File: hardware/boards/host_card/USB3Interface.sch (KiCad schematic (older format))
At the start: 12 parts, among them J2 USB3_Micro_B_Amphenol, J5 Conn_02x04_Odd_Even, U1 ECP5UM5G-381caBGA, U3 CYUSB3014, U6 128MiB

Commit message: Fixed  / updated the ECP5 symbol for the ECP5UM5G-85K
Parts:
- U1: symbol lethalbit:ECP5UM5G-381caBGA -> lethalbit:LFE5UM5G-85F-8BG381I
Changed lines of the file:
@@
 Wire Wire Line
 	5300 6250 5300 6400
-Wire Bus Line
-	3150 3400 3150 4950
-Wire Bus Line
-	9000 2000 9000 3550
 Text Label 11900 2350 2    50   ~ 0
 ALE
@@
 	9000 2000 8650 2000
 $Comp
-L lethalbit:ECP5UM5G-381caBGA U?
+L lethalbit:LFE5UM5G-85F-8BG381I U?
 U 7 1 5FD58016
 P 10450 2200
@@
 NoConn ~ 11350 3550
 NoConn ~ 11350 3650
+Wire Bus Line
+	3150 3400 3150 4950
+Wire Bus Line
+	9000 2000 9000 3550
 $EndSCHEMATC

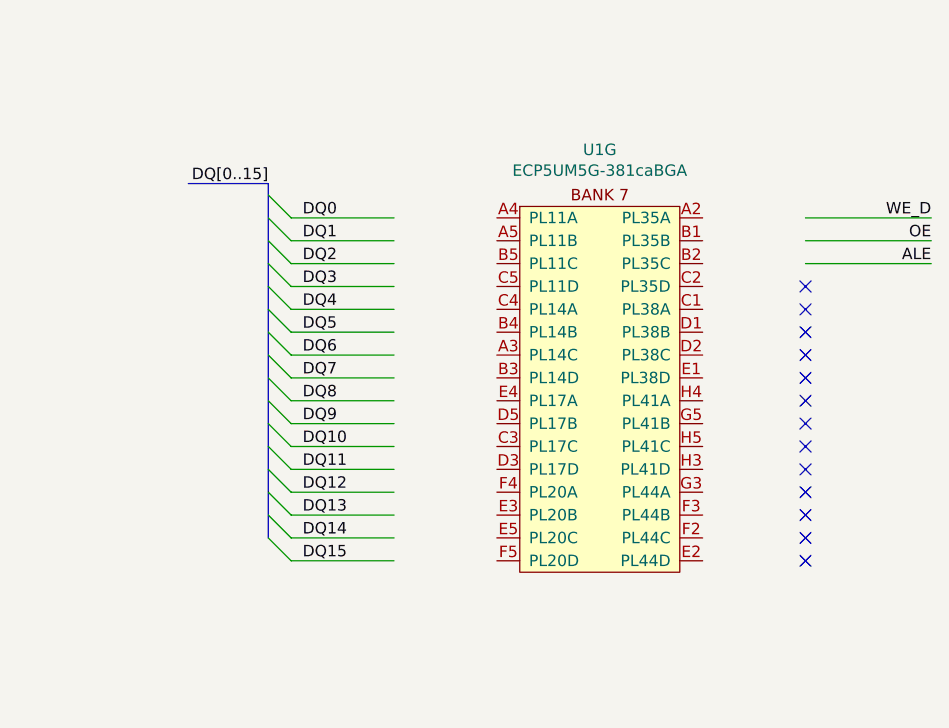
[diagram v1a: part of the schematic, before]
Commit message: Fixed the missing bus connections to the FPGA for the USB3 PHY, and updated the PCB
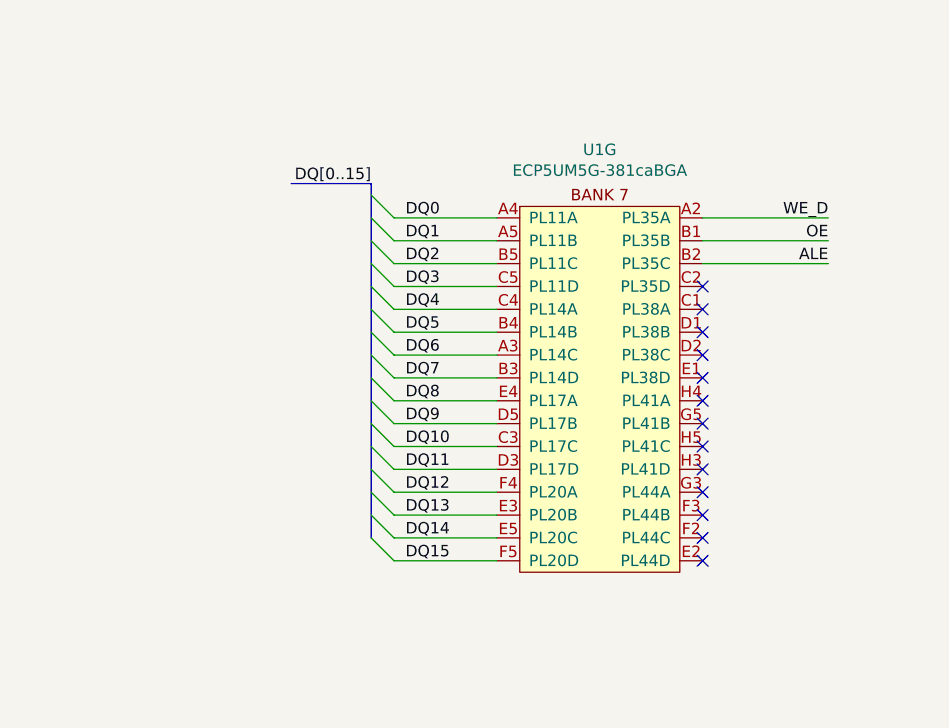
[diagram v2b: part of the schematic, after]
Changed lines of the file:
@@
 Wire Wire Line
 	5300 6250 5300 6400
-Text Label 11900 2350 2    50   ~ 0
+Text Label 11450 2350 2    50   ~ 0
 ALE
 Wire Wire Line
-	11350 2350 11900 2350
-Text Label 11900 2250 2    50   ~ 0
+	10900 2350 11450 2350
+Text Label 11450 2250 2    50   ~ 0
 OE
-Text Label 11900 2150 2    50   ~ 0
+Text Label 11450 2150 2    50   ~ 0
 WE_D
 Wire Wire Line
-	11350 2150 11900 2150
+	10900 2150 11450 2150
 Wire Wire Line
-	11350 2250 11900 2250
-Text Label 9150 2150 0    50   ~ 0
+	10900 2250 11450 2250
+Text Label 9600 2150 0    50   ~ 0
 DQ0
-Text Label 9150 2250 0    50   ~ 0
+Text Label 9600 2250 0    50   ~ 0
 DQ1
-Text Label 9150 2350 0    50   ~ 0
+Text Label 9600 2350 0    50   ~ 0
 DQ2
-Text Label 9150 2450 0    50   ~ 0
+Text Label 9600 2450 0    50   ~ 0
 DQ3
-Text Label 9150 2550 0    50   ~ 0
+Text Label 9600 2550 0    50   ~ 0
 DQ4
-Text Label 9150 2650 0    50   ~ 0
+Text Label 9600 2650 0    50   ~ 0
 DQ5
-Text Label 9150 2750 0    50   ~ 0
+Text Label 9600 2750 0    50   ~ 0
 DQ6
-Text Label 9150 2850 0    50   ~ 0
+Text Label 9600 2850 0    50   ~ 0
 DQ7
-Text Label 9150 2950 0    50   ~ 0
+Text Label 9600 2950 0    50   ~ 0
 DQ8
-Text Label 9150 3050 0    50   ~ 0
+Text Label 9600 3050 0    50   ~ 0
 DQ9
-Text Label 9150 3150 0    50   ~ 0
+Text Label 9600 3150 0    50   ~ 0
 DQ10
-Text Label 9150 3250 0    50   ~ 0
+Text Label 9600 3250 0    50   ~ 0
 DQ11
-Text Label 9150 3350 0    50   ~ 0
+Text Label 9600 3350 0    50   ~ 0
 DQ12
-Text Label 9150 3450 0    50   ~ 0
+Text Label 9600 3450 0    50   ~ 0
 DQ13
-Text Label 9150 3550 0    50   ~ 0
+Text Label 9600 3550 0    50   ~ 0
 DQ14
-Text Label 9150 3650 0    50   ~ 0
+Text Label 9600 3650 0    50   ~ 0
 DQ15
 Wire Wire Line
-	9550 3650 9100 3650
+	10000 3650 9550 3650
 Wire Wire Line
-	9550 3550 9100 3550
+	10000 3550 9550 3550
 Wire Wire Line
-	9550 3450 9100 3450
+	10000 3450 9550 3450
 Wire Wire Line
-	9550 3350 9100 3350
+	10000 3350 9550 3350
 Wire Wire Line
-	9550 3250 9100 3250
+	10000 3250 9550 3250
 Wire Wire Line
-	9550 3150 9100 3150
+	10000 3150 9550 3150
 Wire Wire Line
-	9550 3050 9100 3050
+	10000 3050 9550 3050
 Wire Wire Line
-	9550 2950 9100 2950
+	10000 2950 9550 2950
 Wire Wire Line
-	9550 2850 9100 2850
+	10000 2850 9550 2850
 Wire Wire Line
-	9550 2750 9100 2750
+	10000 2750 9550 2750
 Wire Wire Line
-	9550 2650 9100 2650
+	10000 2650 9550 2650
 Wire Wire Line
-	9550 2550 9100 2550
+	10000 2550 9550 2550
 Wire Wire Line
-	9550 2450 9100 2450
+	10000 2450 9550 2450
 Wire Wire Line
-	9550 2350 9100 2350
+	10000 2350 9550 2350
 Wire Wire Line
-	9550 2250 9100 2250
+	10000 2250 9550 2250
 Wire Wire Line
-	9550 2150 9100 2150
-Text Label 9000 2000 2    50   ~ 0
+	10000 2150 9550 2150
+Text Label 9450 2000 2    50   ~ 0
 DQ[0..15]
 Wire Bus Line
-	9000 2000 8650 2000
+	9450 2000 9100 2000
 $Comp
 L lethalbit:LFE5UM5G-85F-8BG381I U?
@@
 $EndComp
 Entry Wire Line
-	9000 2050 9100 2150
+	9450 2050 9550 2150
 Entry Wire Line
-	9000 2150 9100 2250
+	9450 2150 9550 2250
 Entry Wire Line
-	9000 2250 9100 2350
+	9450 2250 9550 2350
 Entry Wire Line
-	9000 2350 9100 2450
+	9450 2350 9550 2450
 Entry Wire Line
-	9000 2450 9100 2550
+	9450 2450 9550 2550
 Entry Wire Line
-	9000 2550 9100 2650
+	9450 2550 9550 2650
 Entry Wire Line
-	9000 2650 9100 2750
+	9450 2650 9550 2750
 Entry Wire Line
-	9000 2750 9100 2850
+	9450 2750 9550 2850
 Entry Wire Line
-	9000 2850 9100 2950
+	9450 2850 9550 2950
 Entry Wire Line
-	9000 2950 9100 3050
+	9450 2950 9550 3050
 Entry Wire Line
-	9000 3050 9100 3150
+	9450 3050 9550 3150
 Entry Wire Line
-	9000 3150 9100 3250
+	9450 3150 9550 3250
 Entry Wire Line
-	9000 3250 9100 3350
+	9450 3250 9550 3350
 Entry Wire Line
-	9000 3350 9100 3450
+	9450 3350 9550 3450
 Entry Wire Line
-	9000 3450 9100 3550
+	9450 3450 9550 3550
 Entry Wire Line
-	9000 3550 9100 3650
-NoConn ~ 11350 2450
-NoConn ~ 11350 2550
-NoConn ~ 11350 2650
-NoConn ~ 11350 2750
-NoConn ~ 11350 2850
-NoConn ~ 11350 2950
-NoConn ~ 11350 3050
-NoConn ~ 11350 3150
-NoConn ~ 11350 3250
-NoConn ~ 11350 3350
-NoConn ~ 11350 3450
-NoConn ~ 11350 3550
-NoConn ~ 11350 3650
+	9450 3550 9550 3650
+NoConn ~ 10900 2450
+NoConn ~ 10900 2550
+NoConn ~ 10900 2650
+NoConn ~ 10900 2750
+NoConn ~ 10900 2850
+NoConn ~ 10900 2950
+NoConn ~ 10900 3050
+NoConn ~ 10900 3150
+NoConn ~ 10900 3250
+NoConn ~ 10900 3350
+NoConn ~ 10900 3450
+NoConn ~ 10900 3550
+NoConn ~ 10900 3650
 Wire Bus Line
 	3150 3400 3150 4950
 Wire Bus Line
-	9000 2000 9000 3550
+	9450 2000 9450 3550
 $EndSCHEMATC

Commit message: Swizzled the pins on the PHY bus to make routing to the FPGA nicer, also did the initial bus routing
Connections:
- net ALE: now also U1.E1 (PL38D); no longer U1.B2 (PL35C)
- net DQ1: now also U1.C5 (PL11D); no longer U1.A5 (PL11B)
- net DQ10: now also U1.A2 (PL35A); no longer U1.C3 (PL17C)
- net DQ11: now also U1.B1 (PL35B); no longer U1.D3 (PL17D)
- net DQ12: now also U1.B2 (PL35C); no longer U1.F4 (PL20A)
- net DQ13: now also U1.C2 (PL35D); no longer U1.E3 (PL20B)
- net DQ14: now also U1.E3 (PL20B); no longer U1.E5 (PL20C)
- net DQ15: now also U1.D3 (PL17D); no longer U1.F5 (PL20D)
- net DQ2: now also U1.E4 (PL17A); no longer U1.B5 (PL11C)
- net DQ3: now also U1.B4 (PL14B); no longer U1.C5 (PL11D)
- net DQ4: now also U1.D5 (PL17B); no longer U1.C4 (PL14A)
- net DQ5: now also U1.C3 (PL17C); no longer U1.B4 (PL14B)
- net DQ7: now also U1.C4 (PL14A); no longer U1.B3 (PL14D)
- net DQ8: now also U1.B3 (PL14D); no longer U1.E4 (PL17A)
- net DQ9: now also U1.C1 (PL38A); no longer U1.D5 (PL17B)
- net OE: now also U1.E2 (PL44D); no longer U1.B1 (PL35B)
- net WE_D: now also U1.D1 (PL38B); no longer U1.A2 (PL35A)
- net ~PHY_INT: now also U1.D2 (PL38C); no longer U3.K8 (GPIO[17])
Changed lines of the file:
@@
 $EndComp
 Connection ~ 1050 700
-Text HLabel 3450 5250 0    39   Input ~ 0
+Text HLabel 11150 2750 2    39   Input ~ 0
 ~PHY_INT
 $Comp
@@
 DQ0
 Wire Wire Line
-	3450 5250 3700 5250
+	11150 2750 10900 2750
 Wire Wire Line
 	5500 5800 5500 5850
@@
 Wire Wire Line
 	5300 6250 5300 6400
-Text Label 11450 2350 2    50   ~ 0
+Text Label 11450 2850 2    50   ~ 0
 ALE
 Wire Wire Line
-	10900 2350 11450 2350
-Text Label 11450 2250 2    50   ~ 0
+	10900 2850 11450 2850
+Text Label 11450 3650 2    50   ~ 0
 OE
-Text Label 11450 2150 2    50   ~ 0
+Text Label 11450 2650 2    50   ~ 0
 WE_D
 Wire Wire Line
-	10900 2150 11450 2150
-Wire Wire Line
-	10900 2250 11450 2250
+	10900 3650 11450 3650
 Text Label 9600 2150 0    50   ~ 0
 DQ0
-Text Label 9600 2250 0    50   ~ 0
-DQ1
-Text Label 9600 2350 0    50   ~ 0
+Text Label 9600 2950 0    50   ~ 0
 DQ2
-Text Label 9600 2450 0    50   ~ 0
+Text Label 9600 2650 0    50   ~ 0
 DQ3
-Text Label 9600 2550 0    50   ~ 0
+Text Label 9600 3050 0    50   ~ 0
 DQ4
-Text Label 9600 2650 0    50   ~ 0
+Text Label 9600 3150 0    50   ~ 0
 DQ5
 Text Label 9600 2750 0    50   ~ 0
 DQ6
+Text Label 9600 2550 0    50   ~ 0
+DQ7
 Text Label 9600 2850 0    50   ~ 0
-DQ7
-Text Label 9600 2950 0    50   ~ 0
 DQ8
-Text Label 9600 3050 0    50   ~ 0
+Text Label 11000 2550 0    50   ~ 0
 DQ9
-Text Label 9600 3150 0    50   ~ 0
+Text Label 11000 2150 0    50   ~ 0
 DQ10
+Text Label 11000 2250 0    50   ~ 0
+DQ11
+Text Label 11000 2350 0    50   ~ 0
+DQ12
+Text Label 11000 2450 0    50   ~ 0
+DQ13
 Text Label 9600 3250 0    50   ~ 0
-DQ11
-Text Label 9600 3350 0    50   ~ 0
-DQ12
-Text Label 9600 3450 0    50   ~ 0
-DQ13
-Text Label 9600 3550 0    50   ~ 0
-DQ14
-Text Label 9600 3650 0    50   ~ 0
 DQ15
 Wire Wire Line
-	10000 3650 9550 3650
-Wire Wire Line
-	10000 3550 9550 3550
-Wire Wire Line
-	10000 3450 9550 3450
-Wire Wire Line
-	10000 3350 9550 3350
-Wire Wire Line
 	10000 3250 9550 3250
 Wire Wire Line
+	11550 2450 10900 2450
+Wire Wire Line
+	10900 2350 11550 2350
+Wire Wire Line
+	11550 2250 10900 2250
+Wire Wire Line
+	10900 2150 11550 2150
+Wire Wire Line
+	10900 2550 11550 2550
+Wire Wire Line
+	10000 2850 9550 2850
+Wire Wire Line
+	10000 2550 9550 2550
+Wire Wire Line
+	10000 2750 9550 2750
+Wire Wire Line
 	10000 3150 9550 3150
 Wire Wire Line
 	10000 3050 9550 3050
 Wire Wire Line
+	10000 2650 9550 2650
+Wire Wire Line
 	10000 2950 9550 2950
-Wire Wire Line
-	10000 2850 9550 2850
-Wire Wire Line
-	10000 2750 9550 2750
-Wire Wire Line
-	10000 2650 9550 2650
-Wire Wire Line
-	10000 2550 9550 2550
-Wire Wire Line
-	10000 2450 9550 2450
-Wire Wire Line
-	10000 2350 9550 2350
-Wire Wire Line
-	10000 2250 9550 2250
 Wire Wire Line
 	10000 2150 9550 2150
@@
 	9450 2050 9550 2150
 Entry Wire Line
-	9450 2150 9550 2250
-Entry Wire Line
-	9450 2250 9550 2350
-Entry Wire Line
-	9450 2350 9550 2450
+	9450 2850 9550 2950
+Entry Wire Line
+	9450 2550 9550 2650
+Entry Wire Line
+	9450 2950 9550 3050
 Entry Wire Line
 	9450 2450 9550 2550
 Entry Wire Line
-	9450 2550 9550 2650
-Entry Wire Line
 	9450 2650 9550 2750
 Entry Wire Line
+	9450 3050 9550 3150
+Entry Wire Line
 	9450 2750 9550 2850
 Entry Wire Line
-	9450 2850 9550 2950
-Entry Wire Line
-	9450 2950 9550 3050
-Entry Wire Line
-	9450 3050 9550 3150
+	11650 2450 11550 2550
+Entry Wire Line
+	11650 2050 11550 2150
+Entry Wire Line
+	11650 2150 11550 2250
+Entry Wire Line
+	11650 2250 11550 2350
+Entry Wire Line
+	12800 2800 12700 2900
 Entry Wire Line
 	9450 3150 9550 3250
-Entry Wire Line
-	9450 3250 9550 3350
-Entry Wire Line
-	9450 3350 9550 3450
-Entry Wire Line
-	9450 3450 9550 3550
-Entry Wire Line
-	9450 3550 9550 3650
-NoConn ~ 10900 2450
-NoConn ~ 10900 2550
-NoConn ~ 10900 2650
-NoConn ~ 10900 2750
-NoConn ~ 10900 2850
+NoConn ~ 3700 5250
 NoConn ~ 10900 2950
 NoConn ~ 10900 3050
@@
 NoConn ~ 10900 3450
 NoConn ~ 10900 3550
-NoConn ~ 10900 3650
+Text Label 11650 2000 0    50   ~ 0
+DQ[0..15]
+Wire Bus Line
+	11650 2000 12000 2000
+Entry Wire Line
+	11650 2350 11550 2450
+Wire Wire Line
+	10900 2650 11450 2650
+Entry Wire Line
+	9450 3350 9550 3450
+Wire Wire Line
+	10000 3450 9550 3450
+Text Label 9600 3450 0    50   ~ 0
+DQ14
+Entry Wire Line
+	9450 2350 9550 2450
+Wire Wire Line
+	10000 2450 9550 2450
+Text Label 9600 2450 0    50   ~ 0
+DQ1
+NoConn ~ 10000 2250
+NoConn ~ 10000 2350
+NoConn ~ 10000 3350
+NoConn ~ 10000 3550
+NoConn ~ 10000 3650
+Wire Bus Line
+	11650 2000 11650 2450
+Wire Bus Line
+	9450 2000 9450 3350
 Wire Bus Line
 	3150 3400 3150 4950
-Wire Bus Line
-	9450 2000 9450 3550
 $EndSCHEMATC

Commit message: Wiggling traces is hard
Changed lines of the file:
@@
 	11650 2250 11550 2350
-Entry Wire Line
-	12800 2800 12700 2900
 Entry Wire Line
 	9450 3150 9550 3250

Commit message: Lots of updates from a while ago, don't recall what's changed
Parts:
- J5: MFR (none) -> Samtec; MPN (none) -> FTSH-105-01-L-DV-K-TR
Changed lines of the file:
@@
 F 2 "lethalbit-connectors:FTSH-105-01-L-DV-K-TR" H 6450 6800 50  0001 C CNN
 F 3 "~" H 6450 6800 50  0001 C CNN
+F 4 "Samtec" H 6450 6800 50  0001 C CNN "MFR"
+F 5 "FTSH-105-01-L-DV-K-TR" H 6450 6800 50  0001 C CNN "MPN"
 	1    6450 6800
 	-1   0    0    1
